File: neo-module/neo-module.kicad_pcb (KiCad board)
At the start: 2 copper layers, 80 x 22 mm, 18 parts

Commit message: move mounting holes on modules and controller
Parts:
- added ?: , , F.Cu at (178.0, 99.0)
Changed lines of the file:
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@@
 		)
+	)
+	(footprint ""
+		(layer "F.Cu")
+		(at 178 99)
+		(property "Reference" ""
+			(at 0 0 0)
+			(layer "F.SilkS")
+			(effects
+				(font
+					(size 1.27 1.27)
+					(thickness 0.15)
+				)
+			)
+		)
+		(property "Value" ""
+			(at 0 0 0)
+			(layer "F.Fab")
+			(effects
+				(font
+					(size 1.27 1.27)
+					(thickness 0.15)
+				)
+			)
+		)
+		(property "Datasheet" ""
+			(at 0 0 0)
+			(layer "F.Fab")
+			(hide yes)
+			(effects
+				(font
+					(size 1.27 1.27)
+					(thickness 0.15)
+				)
+			)
+		)
+		(property "Description" ""
+			(at 0 0 0)
+			(layer "F.Fab")
+			(hide yes)
+			(effects
+				(font
+					(size 1.27 1.27)
+					(thickness 0.15)
+				)
+			)
+		)
+		(pad "" np_thru_hole circle
+			(at -13 7)
+			(size 2.9 2.9)
+			(drill 2.9)
+			(layers "*.Cu" "*.Mask")
+		)
+		(embedded_fonts no)
 	)
 	(footprint "ProjectDMX:Vert Terminal Block p3"

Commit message: adjust footprints and cleanup stuff
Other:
- board text added: "A: 1011"
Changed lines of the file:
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@@
 		(layer "Edge.Cuts")
+	)
+	(gr_text "A: 1011"
+		(at 142 101 0)
+		(layer "F.SilkS")
+		(effects
+			(font
+				(size 1 1)
+				(thickness 0.25)
+				(bold yes)
+			)
+		)
 	)
 	(gr_text "3 Pin Neo Driver v1\nprojectdmx.com"

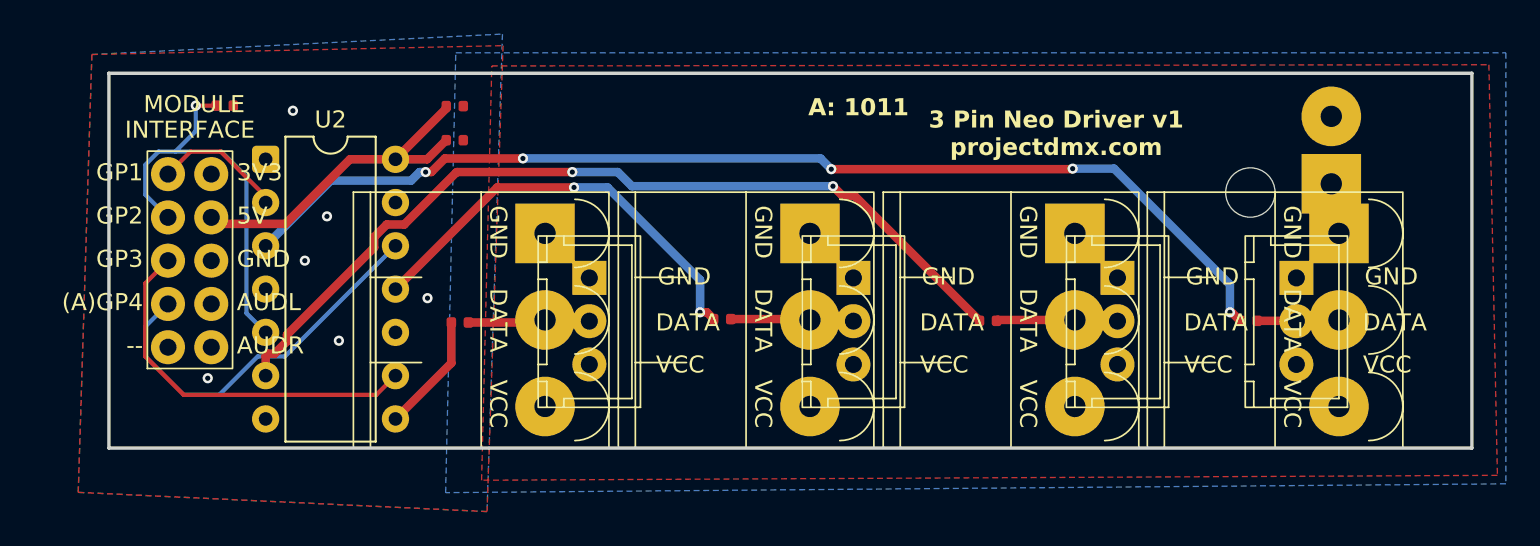
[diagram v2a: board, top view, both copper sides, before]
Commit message: update footprints on neo module
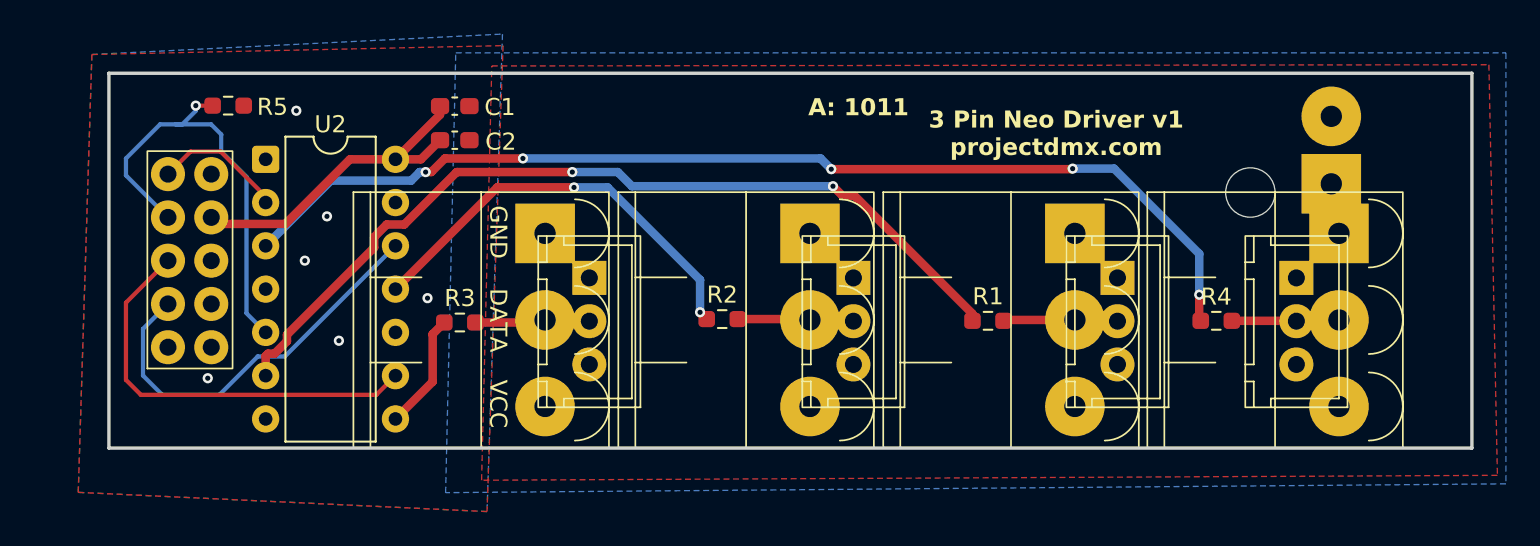
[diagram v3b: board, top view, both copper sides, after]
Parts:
- C1, C2: footprint PCM_JLCPCB:C_0402 -> Capacitor_SMD:C_0603_1608Metric_Pad1.08x0.95mm_HandSolder
- R1, R2, R3, R4, R5: footprint PCM_JLCPCB:R_0402 -> Resistor_SMD:R_0603_1608Metric_Pad0.98x0.95mm_HandSolder
- moved R4 1.90 mm to (163.0, 113.5)
- moved R5 0.20 mm to (105.0, 100.9)
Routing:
- net Net-(U1-GP3): track 22.3 -> 24.7 mm
- net Net-(U1-GP2): track 24.5 -> 26.9 mm
- net Net-(U1-AGP4): track 22.9 -> 23.7 mm
- net Net-(U2-2Y_(Out)): track 30.1 -> 29.3 mm
- net Net-(U2-1Y_(Out)): track 11.6 -> 11.0 mm
- net Net-(U2-3Y_(Out)): track 56.4 -> 55.8 mm
- net 5V: track 20.3 -> 19.8 mm

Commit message: cleanup footprints and layout
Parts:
- moved REF** 0.45 mm to (167.7, 108.0)
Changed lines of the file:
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@@
 	(footprint "ProjectDMX:JST VH"
 		(layer "B.Cu")
-		(at 167.25 107.95)
+		(at 167.7 107.95)
 		(property "Reference" "REF**"
 			(at 0 0.5 180)
@@
 	)
 	(gr_text "A: 1011"
-		(at 142 101 0)
+		(at 99.327659 110.046453 90)
 		(layer "F.SilkS")
 		(effects
@@
 	)
 	(gr_text "3 Pin Neo Driver v1\nprojectdmx.com"
-		(at 153.6 102.53 0)
+		(at 153.6 102 0)
 		(layer "F.SilkS")
 		(effects
